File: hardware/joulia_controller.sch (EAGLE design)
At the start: 42 parts, among them IC1 LM2902D, IC2 LM2902D, U1 MMBT2222ALT1G, U2 MMBT2222ALT1G

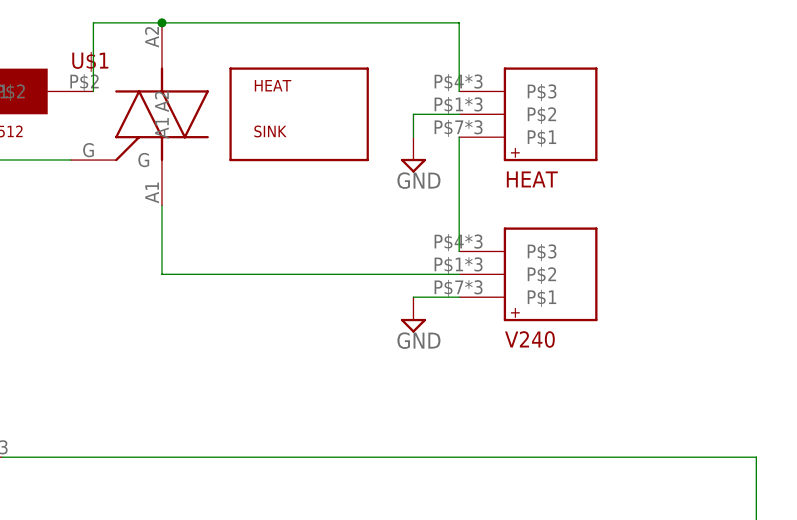
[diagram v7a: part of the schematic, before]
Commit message: Switches two plugs for one board terminal for 240V connections.
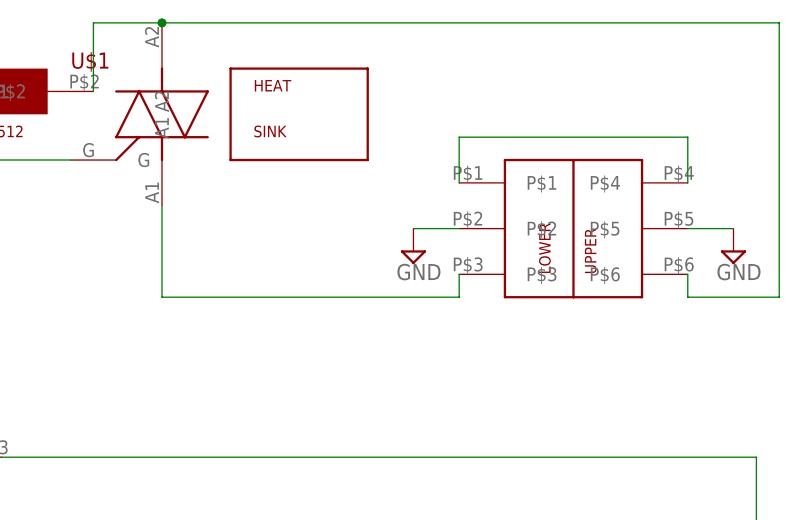
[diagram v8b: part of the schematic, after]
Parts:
- removed HEAT, V240: PC1720589, digikey:PC1720589
- added U$6: PC1719028, digikey:PC1719028
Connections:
- net +120: now also U$6.P$1, U$6.P$4; no longer HEAT.P$1, V240.P$3
- net -120: now also U$6.P$3; no longer V240.P$2
- net GND: now also U$6.P$2, U$6.P$5; no longer HEAT.P$2, V240.P$1
- net N$22: now also U$6.P$6; no longer HEAT.P$3
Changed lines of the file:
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@@
 <part name="P+1" library="supply1" library_urn="urn:adsk.eagle:library:371" deviceset="+5V" device=""/>
 <part name="P+2" library="supply1" library_urn="urn:adsk.eagle:library:371" deviceset="+5V" device=""/>
-<part name="HEAT" library="digikey" deviceset="PC1720589" device=""/>
 <part name="SUPPLY17" library="supply2" library_urn="urn:adsk.eagle:library:372" deviceset="GND" device=""/>
 <part name="SUPPLY18" library="supply2" library_urn="urn:adsk.eagle:library:372" deviceset="GND" device=""/>
-<part name="V240" library="digikey" deviceset="PC1720589" device=""/>
 <part name="SUPPLY19" library="supply2" library_urn="urn:adsk.eagle:library:372" deviceset="GND" device=""/>
 <part name="R17" library="resistor" library_urn="urn:adsk.eagle:library:348" deviceset="R-US_" device="R1206" value="330"/>
@@
 <part name="D1" library="diode" library_urn="urn:adsk.eagle:library:210" deviceset="CGRM400*-G" device="" technology="1"/>
 <part name="U$4" library="digikey" deviceset="PC1725041" device=""/>
+<part name="U$6" library="digikey" deviceset="PC1719028" device=""/>
 </parts>
 <sheets>
@@
 <instance part="P+1" gate="1" x="243.84" y="132.08"/>
 <instance part="P+2" gate="1" x="256.54" y="93.98"/>
-<instance part="HEAT" gate="G$1" x="332.74" y="124.46" rot="MR180"/>
-<instance part="SUPPLY17" gate="GND" x="322.58" y="119.38"/>
+<instance part="SUPPLY17" gate="GND" x="358.14" y="109.22"/>
 <instance part="SUPPLY18" gate="GND" x="358.14" y="53.34"/>
-<instance part="V240" gate="G$1" x="332.74" y="106.68" rot="MR180"/>
-<instance part="SUPPLY19" gate="GND" x="322.58" y="101.6"/>
+<instance part="SUPPLY19" gate="GND" x="322.58" y="109.22"/>
 <instance part="R17" gate="G$1" x="243.84" y="111.76" rot="R90"/>
 <instance part="HELED" gate="G$1" x="185.42" y="88.9"/>
@@
 <instance part="D1" gate="G$1" x="243.84" y="81.28" rot="R90"/>
 <instance part="U$4" gate="G$1" x="340.36" y="55.88"/>
+<instance part="U$6" gate="G$1" x="340.36" y="111.76"/>
 </instances>
 <busses>
@@
 </segment>
 <segment>
-<pinref part="HEAT" gate="G$1" pin="P$2"/>
-<wire x1="327.66" y1="124.46" x2="322.58" y2="124.46" width="0.1524" layer="91"/>
-<wire x1="322.58" y1="124.46" x2="322.58" y2="121.92" width="0.1524" layer="91"/>
+<wire x1="353.06" y1="111.76" x2="358.14" y2="111.76" width="0.1524" layer="91"/>
 <pinref part="SUPPLY17" gate="GND" pin="GND"/>
+<pinref part="U$6" gate="G$1" pin="P$5"/>
 </segment>
 <segment>
@@
 </segment>
 <segment>
-<pinref part="V240" gate="G$1" pin="P$1"/>
 <pinref part="SUPPLY19" gate="GND" pin="GND"/>
-<wire x1="327.66" y1="104.14" x2="322.58" y2="104.14" width="0.1524" layer="91"/>
+<wire x1="327.66" y1="111.76" x2="322.58" y2="111.76" width="0.1524" layer="91"/>
+<pinref part="U$6" gate="G$1" pin="P$2"/>
 </segment>
 <segment>
@@
 <pinref part="U$1" gate="G$1" pin="A2"/>
 <wire x1="287.02" y1="134.62" x2="294.64" y2="134.62" width="0.1524" layer="91"/>
-<pinref part="HEAT" gate="G$1" pin="P$3"/>
-<wire x1="327.66" y1="127" x2="327.66" y2="134.62" width="0.1524" layer="91"/>
-<wire x1="327.66" y1="134.62" x2="294.64" y2="134.62" width="0.1524" layer="91"/>
+<wire x1="353.06" y1="106.68" x2="353.06" y2="104.14" width="0.1524" layer="91"/>
+<wire x1="353.06" y1="104.14" x2="363.22" y2="104.14" width="0.1524" layer="91"/>
+<wire x1="363.22" y1="104.14" x2="363.22" y2="134.62" width="0.1524" layer="91"/>
+<wire x1="363.22" y1="134.62" x2="294.64" y2="134.62" width="0.1524" layer="91"/>
 <junction x="294.64" y="134.62"/>
+<pinref part="U$6" gate="G$1" pin="P$6"/>
 </segment>
 </net>
@@
 <net name="-120" class="2">
 <segment>
-<pinref part="V240" gate="G$1" pin="P$2"/>
 <pinref part="U$1" gate="G$1" pin="A1"/>
-<wire x1="327.66" y1="106.68" x2="294.64" y2="106.68" width="0.1524" layer="91"/>
-<wire x1="294.64" y1="106.68" x2="294.64" y2="114.3" width="0.1524" layer="91"/>
+<wire x1="294.64" y1="114.3" x2="294.64" y2="104.14" width="0.1524" layer="91"/>
+<pinref part="U$6" gate="G$1" pin="P$3"/>
+<wire x1="294.64" y1="104.14" x2="327.66" y2="104.14" width="0.1524" layer="91"/>
+<wire x1="327.66" y1="104.14" x2="327.66" y2="106.68" width="0.1524" layer="91"/>
 </segment>
 </net>
 <net name="+120" class="2">
 <segment>
-<pinref part="HEAT" gate="G$1" pin="P$1"/>
-<pinref part="V240" gate="G$1" pin="P$3"/>
-<wire x1="327.66" y1="121.92" x2="327.66" y2="109.22" width="0.1524" layer="91"/>
-</segment>
-</net>
+<wire x1="353.06" y1="116.84" x2="353.06" y2="121.92" width="0.1524" layer="91"/>
+<wire x1="353.06" y1="121.92" x2="327.66" y2="121.92" width="0.1524" layer="91"/>
+<wire x1="327.66" y1="121.92" x2="327.66" y2="116.84" width="0.1524" layer="91"/>
+<pinref part="U$6" gate="G$1" pin="P$1"/>
+<pinref part="U$6" gate="G$1" pin="P$4"/>
+</segment>
+</net>
